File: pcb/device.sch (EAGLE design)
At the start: 19 parts, among them IC1 TINY13-20PU

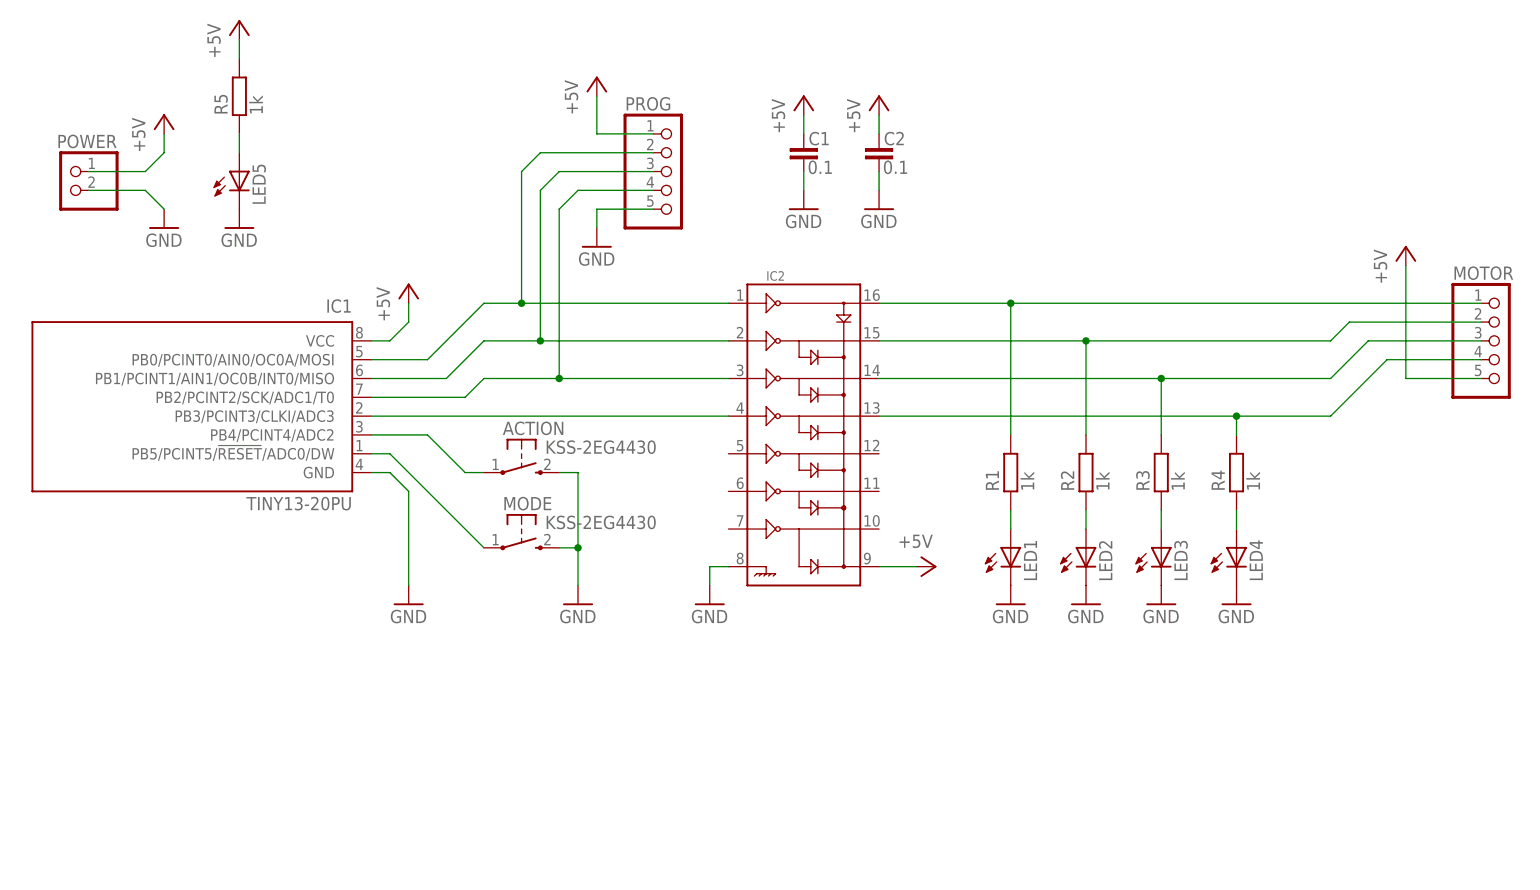
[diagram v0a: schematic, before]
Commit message: Fix motor connection and add pullup on action pin.
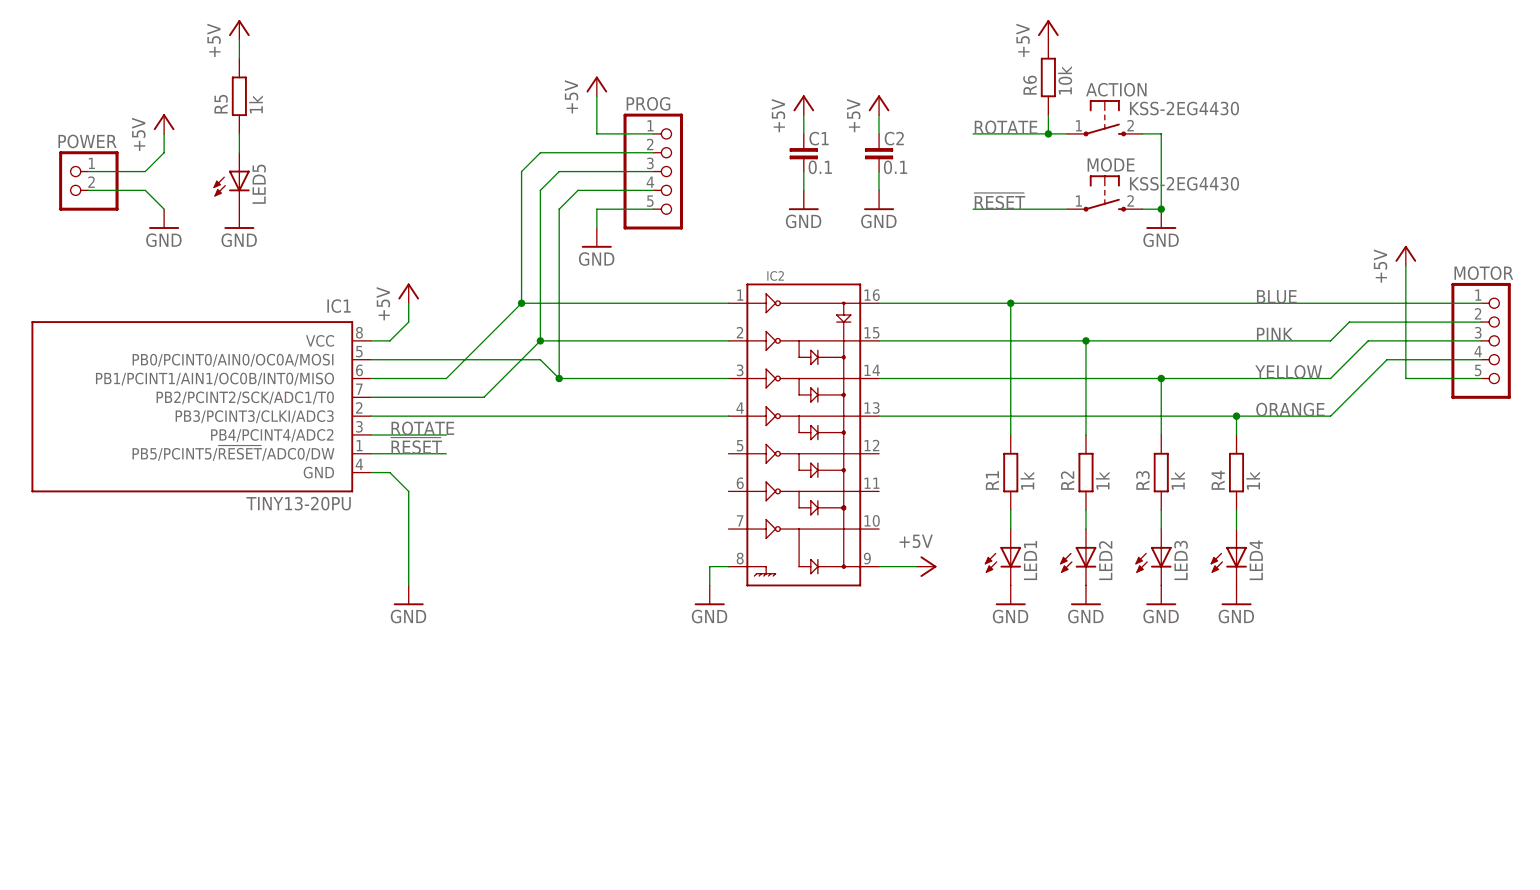
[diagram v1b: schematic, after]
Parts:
- added R6: 10k, rc-master-smd:R_0805
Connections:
- net N$18 renamed !RESET
- removed net N$17: ACTION.P, IC1.PB4/PCINT4/ADC2
- new net ROTATE: ACTION.P, IC1.PB4/PCINT4/ADC2, R6.1
- net +5V: now also R6.2
- net MISO: now also IC1.PB2/PCINT2/SCK/ADC1/T0; no longer IC1.PB1/PCINT1/AIN1/OC0B/INT0/MISO
- net MOSI: now also IC1.PB1/PCINT1/AIN1/OC0B/INT0/MISO; no longer IC1.PB0/PCINT0/AIN0/OC0A/MOSI
- net SCK: now also IC1.PB0/PCINT0/AIN0/OC0A/MOSI; no longer IC1.PB2/PCINT2/SCK/ADC1/T0
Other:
- moved on the sheet: ACTION, MODE
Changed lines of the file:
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@@
 <part name="GND12" library="supply1" deviceset="GND" device=""/>
 <part name="P+8" library="supply1" deviceset="+5V" device=""/>
+<part name="R6" library="rc-master-smd" deviceset="R_" device="0805" value="10k"/>
+<part name="P+9" library="supply1" deviceset="+5V" device=""/>
 </parts>
 <sheets>
@@
 <instance part="P+4" gate="1" x="10.16" y="73.66"/>
 <instance part="GND8" gate="1" x="10.16" y="58.42"/>
-<instance part="ACTION" gate="G$1" x="-38.1" y="22.86"/>
-<instance part="MODE" gate="G$1" x="-38.1" y="12.7"/>
-<instance part="GND9" gate="1" x="-30.48" y="5.08"/>
+<instance part="ACTION" gate="G$1" x="40.64" y="68.58"/>
+<instance part="MODE" gate="G$1" x="40.64" y="58.42"/>
+<instance part="GND9" gate="1" x="48.26" y="55.88"/>
 <instance part="MOTOR" gate="A" x="93.98" y="40.64"/>
 <instance part="PROG" gate="A" x="-17.78" y="63.5"/>
@@
 <instance part="GND12" gate="1" x="-76.2" y="55.88"/>
 <instance part="P+8" gate="1" x="-76.2" y="83.82"/>
+<instance part="R6" gate="G$1" x="33.02" y="76.2" rot="R90"/>
+<instance part="P+9" gate="1" x="33.02" y="83.82"/>
 </instances>
 <busses>
@@
 <pinref part="P+8" gate="1" pin="+5V"/>
 </segment>
+<segment>
+<pinref part="R6" gate="G$1" pin="2"/>
+<pinref part="P+9" gate="1" pin="+5V"/>
+</segment>
 </net>
 <net name="N$1" class="0">
@@
 <segment>
 <pinref part="MODE" gate="G$1" pin="S"/>
-<wire x1="-33.02" y1="12.7" x2="-30.48" y2="12.7" width="0.1524" layer="91"/>
+<wire x1="45.72" y1="58.42" x2="48.26" y2="58.42" width="0.1524" layer="91"/>
 <pinref part="GND9" gate="1" pin="GND"/>
-<wire x1="-30.48" y1="12.7" x2="-30.48" y2="7.62" width="0.1524" layer="91"/>
 <pinref part="ACTION" gate="G$1" pin="S"/>
-<wire x1="-33.02" y1="22.86" x2="-30.48" y2="22.86" width="0.1524" layer="91"/>
-<wire x1="-30.48" y1="22.86" x2="-30.48" y2="12.7" width="0.1524" layer="91"/>
-<junction x="-30.48" y="12.7"/>
+<wire x1="45.72" y1="68.58" x2="48.26" y2="68.58" width="0.1524" layer="91"/>
+<wire x1="48.26" y1="68.58" x2="48.26" y2="58.42" width="0.1524" layer="91"/>
+<junction x="48.26" y="58.42"/>
 </segment>
 <segment>
@@
 <net name="MOSI" class="0">
 <segment>
-<pinref part="IC1" gate="G$1" pin="PB0/PCINT0/AIN0/OC0A/MOSI"/>
-<wire x1="-58.42" y1="38.1" x2="-50.8" y2="38.1" width="0.1524" layer="91"/>
-<wire x1="-50.8" y1="38.1" x2="-43.18" y2="45.72" width="0.1524" layer="91"/>
 <pinref part="IC2" gate="G$1" pin="1"/>
-<wire x1="-43.18" y1="45.72" x2="-38.1" y2="45.72" width="0.1524" layer="91"/>
 <pinref part="PROG" gate="A" pin="2"/>
 <wire x1="-38.1" y1="45.72" x2="-10.16" y2="45.72" width="0.1524" layer="91"/>
@@
 <wire x1="-35.56" y1="66.04" x2="-38.1" y2="63.5" width="0.1524" layer="91"/>
 <wire x1="-38.1" y1="63.5" x2="-38.1" y2="45.72" width="0.1524" layer="91"/>
-<junction x="-38.1" y="45.72"/>
-</segment>
-</net>
-<net name="MISO" class="0">
-<segment>
 <pinref part="IC1" gate="G$1" pin="PB1/PCINT1/AIN1/OC0B/INT0/MISO"/>
 <wire x1="-58.42" y1="35.56" x2="-48.26" y2="35.56" width="0.1524" layer="91"/>
-<wire x1="-48.26" y1="35.56" x2="-43.18" y2="40.64" width="0.1524" layer="91"/>
+<wire x1="-48.26" y1="35.56" x2="-38.1" y2="45.72" width="0.1524" layer="91"/>
+<junction x="-38.1" y="45.72"/>
+</segment>
+</net>
+<net name="MISO" class="0">
+<segment>
 <pinref part="IC2" gate="G$1" pin="2"/>
-<wire x1="-43.18" y1="40.64" x2="-35.56" y2="40.64" width="0.1524" layer="91"/>
 <pinref part="PROG" gate="A" pin="3"/>
 <wire x1="-35.56" y1="40.64" x2="-10.16" y2="40.64" width="0.1524" layer="91"/>
@@
 <wire x1="-33.02" y1="63.5" x2="-35.56" y2="60.96" width="0.1524" layer="91"/>
 <wire x1="-35.56" y1="60.96" x2="-35.56" y2="40.64" width="0.1524" layer="91"/>
+<pinref part="IC1" gate="G$1" pin="PB2/PCINT2/SCK/ADC1/T0"/>
+<wire x1="-58.42" y1="33.02" x2="-43.18" y2="33.02" width="0.1524" layer="91"/>
+<wire x1="-43.18" y1="33.02" x2="-35.56" y2="40.64" width="0.1524" layer="91"/>
 <junction x="-35.56" y="40.64"/>
 </segment>
@@
 <net name="SCK" class="0">
 <segment>
-<pinref part="IC1" gate="G$1" pin="PB2/PCINT2/SCK/ADC1/T0"/>
-<wire x1="-58.42" y1="33.02" x2="-45.72" y2="33.02" width="0.1524" layer="91"/>
-<wire x1="-45.72" y1="33.02" x2="-43.18" y2="35.56" width="0.1524" layer="91"/>
 <pinref part="IC2" gate="G$1" pin="3"/>
-<wire x1="-43.18" y1="35.56" x2="-33.02" y2="35.56" width="0.1524" layer="91"/>
 <pinref part="PROG" gate="A" pin="4"/>
 <wire x1="-33.02" y1="35.56" x2="-10.16" y2="35.56" width="0.1524" layer="91"/>
@@
 <wire x1="-30.48" y1="60.96" x2="-33.02" y2="58.42" width="0.1524" layer="91"/>
 <wire x1="-33.02" y1="58.42" x2="-33.02" y2="35.56" width="0.1524" layer="91"/>
+<pinref part="IC1" gate="G$1" pin="PB0/PCINT0/AIN0/OC0A/MOSI"/>
+<wire x1="-58.42" y1="38.1" x2="-35.56" y2="38.1" width="0.1524" layer="91"/>
+<wire x1="-35.56" y1="38.1" x2="-33.02" y2="35.56" width="0.1524" layer="91"/>
 <junction x="-33.02" y="35.56"/>
-</segment>
-</net>
-<net name="N$8" class="0">
-<segment>
-<pinref part="IC1" gate="G$1" pin="PB3/PCINT3/CLKI/ADC3"/>
-<pinref part="IC2" gate="G$1" pin="4"/>
-<wire x1="-58.42" y1="30.48" x2="-10.16" y2="30.48" width="0.1524" layer="91"/>
 </segment>
 </net>
@@
 <junction x="27.94" y="45.72"/>
 <pinref part="MOTOR" gate="A" pin="1"/>
+<label x="60.96" y="45.72" size="1.778" layer="95"/>
 </segment>
 </net>
@@
 <pinref part="MOTOR" gate="A" pin="2"/>
 <wire x1="73.66" y1="43.18" x2="91.44" y2="43.18" width="0.1524" layer="91"/>
+<label x="60.96" y="40.64" size="1.778" layer="95"/>
 </segment>
 </net>
@@
 <pinref part="MOTOR" gate="A" pin="3"/>
 <wire x1="76.2" y1="40.64" x2="91.44" y2="40.64" width="0.1524" layer="91"/>
+<label x="60.96" y="35.56" size="1.778" layer="95"/>
 </segment>
 </net>
@@
 <pinref part="MOTOR" gate="A" pin="4"/>
 <wire x1="78.74" y1="38.1" x2="91.44" y2="38.1" width="0.1524" layer="91"/>
-</segment>
-</net>
-<net name="N$17" class="0">
-<segment>
-<pinref part="IC1" gate="G$1" pin="PB4/PCINT4/ADC2"/>
-<wire x1="-58.42" y1="27.94" x2="-50.8" y2="27.94" width="0.1524" layer="91"/>
-<wire x1="-50.8" y1="27.94" x2="-45.72" y2="22.86" width="0.1524" layer="91"/>
-<pinref part="ACTION" gate="G$1" pin="P"/>
-<wire x1="-45.72" y1="22.86" x2="-43.18" y2="22.86" width="0.1524" layer="91"/>
-</segment>
-</net>
-<net name="N$18" class="0">
-<segment>
-<pinref part="IC1" gate="G$1" pin="PB5/PCINT5/!RESET!/ADC0/DW"/>
-<pinref part="MODE" gate="G$1" pin="P"/>
-<wire x1="-58.42" y1="25.4" x2="-55.88" y2="25.4" width="0.1524" layer="91"/>
-<wire x1="-55.88" y1="25.4" x2="-43.18" y2="12.7" width="0.1524" layer="91"/>
+<label x="60.96" y="30.48" size="1.778" layer="95"/>
 </segment>
 </net>
@@
 </segment>
 </net>
+<net name="N$6" class="0">
+<segment>
+<pinref part="IC1" gate="G$1" pin="PB3/PCINT3/CLKI/ADC3"/>
+<pinref part="IC2" gate="G$1" pin="4"/>
+<wire x1="-58.42" y1="30.48" x2="-10.16" y2="30.48" width="0.1524" layer="91"/>
+</segment>
+</net>
+<net name="ROTATE" class="0">
+<segment>
+<pinref part="IC1" gate="G$1" pin="PB4/PCINT4/ADC2"/>
+<wire x1="-58.42" y1="27.94" x2="-48.26" y2="27.94" width="0.1524" layer="91"/>
+<label x="-55.88" y="27.94" size="1.778" layer="95"/>
+</segment>
+<segment>
+<pinref part="ACTION" gate="G$1" pin="P"/>
+<wire x1="35.56" y1="68.58" x2="33.02" y2="68.58" width="0.1524" layer="91"/>
+<label x="22.86" y="68.58" size="1.778" layer="95"/>
+<pinref part="R6" gate="G$1" pin="1"/>
+<wire x1="33.02" y1="68.58" x2="22.86" y2="68.58" width="0.1524" layer="91"/>
+<wire x1="33.02" y1="68.58" x2="33.02" y2="71.12" width="0.1524" layer="91"/>
+<junction x="33.02" y="68.58"/>
+</segment>
+</net>
+<net name="!RESET" class="0">
+<segment>
+<pinref part="IC1" gate="G$1" pin="PB5/PCINT5/!RESET!/ADC0/DW"/>
+<wire x1="-58.42" y1="25.4" x2="-48.26" y2="25.4" width="0.1524" layer="91"/>
+<label x="-55.88" y="25.4" size="1.778" layer="95"/>
+</segment>
+<segment>
+<pinref part="MODE" gate="G$1" pin="P"/>
+<wire x1="35.56" y1="58.42" x2="22.86" y2="58.42" width="0.1524" layer="91"/>
+<label x="22.86" y="58.42" size="1.778" layer="95"/>
+</segment>
+</net>

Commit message: Almost ready PCB.
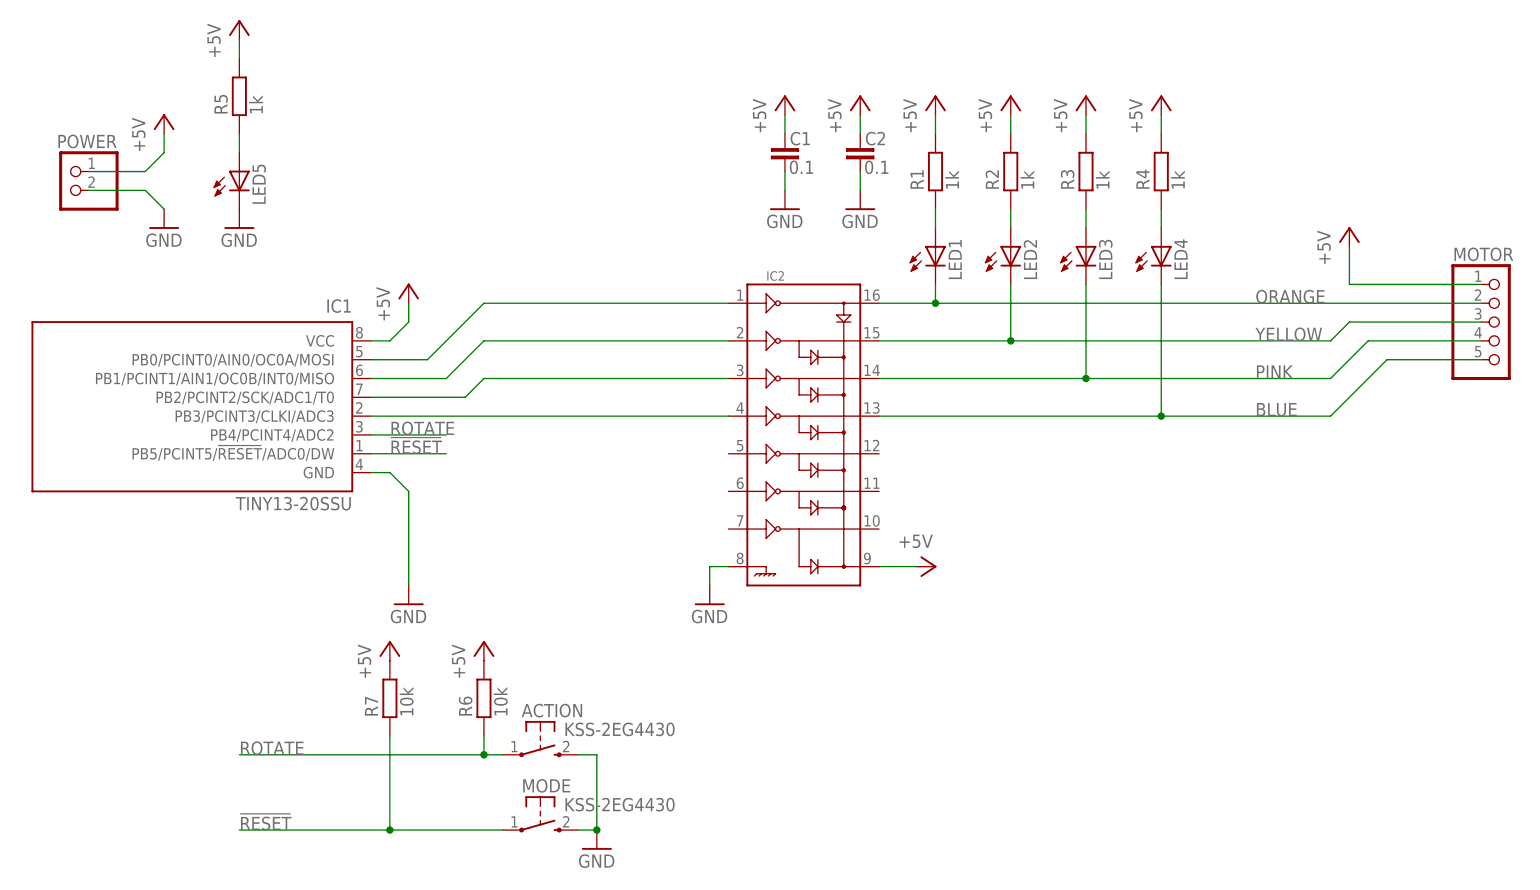
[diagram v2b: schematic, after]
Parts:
- removed PROG: (no value), pinhead-fixdrills:PINHD-1X5_2.54
- added R7: 10k, rc-master-smd:R_0805
- IC1: value TINY13-20PU -> TINY13-20SSU; device avr:TINY13-20PU -> avr:TINY13-20SSU
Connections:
- removed net MISO: IC1.PB2/PCINT2/SCK/ADC1/T0, IC2.2, PROG.3
- removed net MOSI: IC1.PB1/PCINT1/AIN1/OC0B/INT0/MISO, IC2.1, PROG.2
- removed net SCK: IC1.PB0/PCINT0/AIN0/OC0A/MOSI, IC2.3, PROG.4
- new net N$6: IC1.PB0/PCINT0/AIN0/OC0A/MOSI, IC2.1
- new net N$7: IC1.PB1/PCINT1/AIN1/OC0B/INT0/MISO, IC2.2
- new net N$8: IC1.PB2/PCINT2/SCK/ADC1/T0, IC2.3
- net !RESET: now also R7.1
- net +5V: now also MOTOR.1, R1.2, R2.2, R3.2, R4.2, R7.2; no longer MOTOR.5, PROG.1
- net BLUE: now also IC2.13, LED4.C, MOTOR.5; no longer IC2.16, MOTOR.1, R1.2
- net GND: no longer LED1.C, LED2.C, LED3.C, LED4.C, PROG.5
- net ORANGE: now also IC2.16, LED1.C, MOTOR.2; no longer IC2.13, MOTOR.4, R4.2
- net PINK: now also IC2.14, LED3.C, MOTOR.4; no longer IC2.15, MOTOR.2, R2.2
- net YELLOW: now also IC2.15, LED2.C; no longer IC2.14, R3.2
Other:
- moved on the sheet: ACTION, C1, C2, LED1, LED2, LED3, LED4, MODE, MOTOR, R1, R2, R3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
